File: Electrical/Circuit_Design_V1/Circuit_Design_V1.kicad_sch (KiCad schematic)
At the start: 0 parts

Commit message: #3 Improving the coincell battery holder symbol.
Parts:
- added P1: ~, symbol Etchasketch_hardware_symbol_library:20mm_Coin_Cell_Breakout_Board_(CR2032)
- added U1: STM32G474RETx, Package_QFP:LQFP-64_10x10mm_P0.5mm, symbol MCU_ST_STM32G4:STM32G474RETx
- added U2: ~, symbol Etchasketch_hardware_symbol_library:4.2{dblquote}_300x400_Tri-Color_eInk_/_ePap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
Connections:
- new net: U1.15 (VSS), U1.31 (VSS), U1.47 (VSS), U1.63 (VSS)

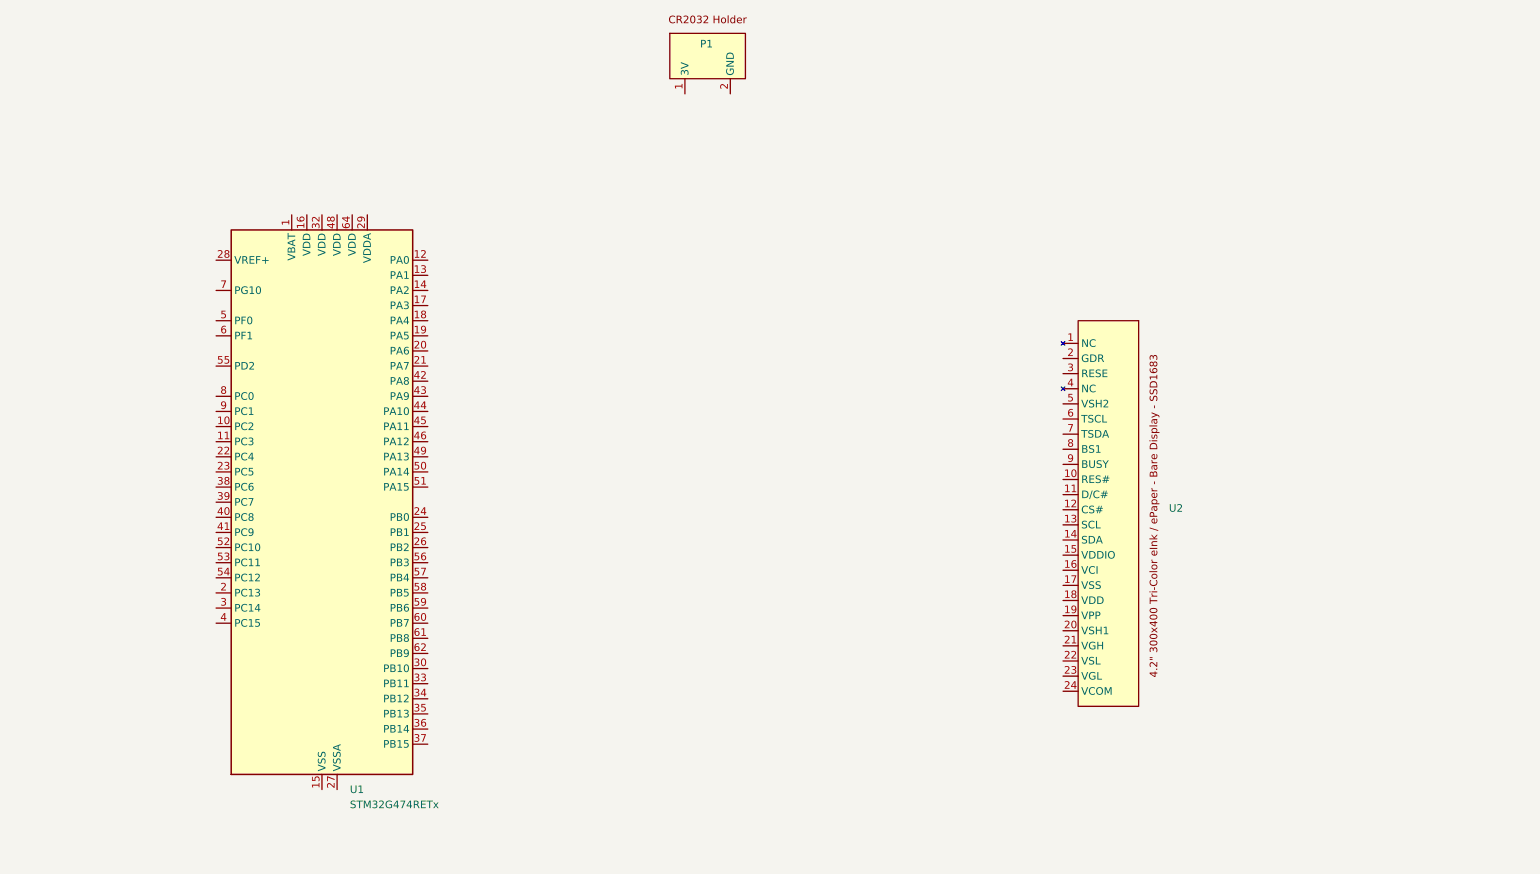
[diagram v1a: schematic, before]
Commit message: #3 Connecting MCU connectors to E-Ink on schematic.
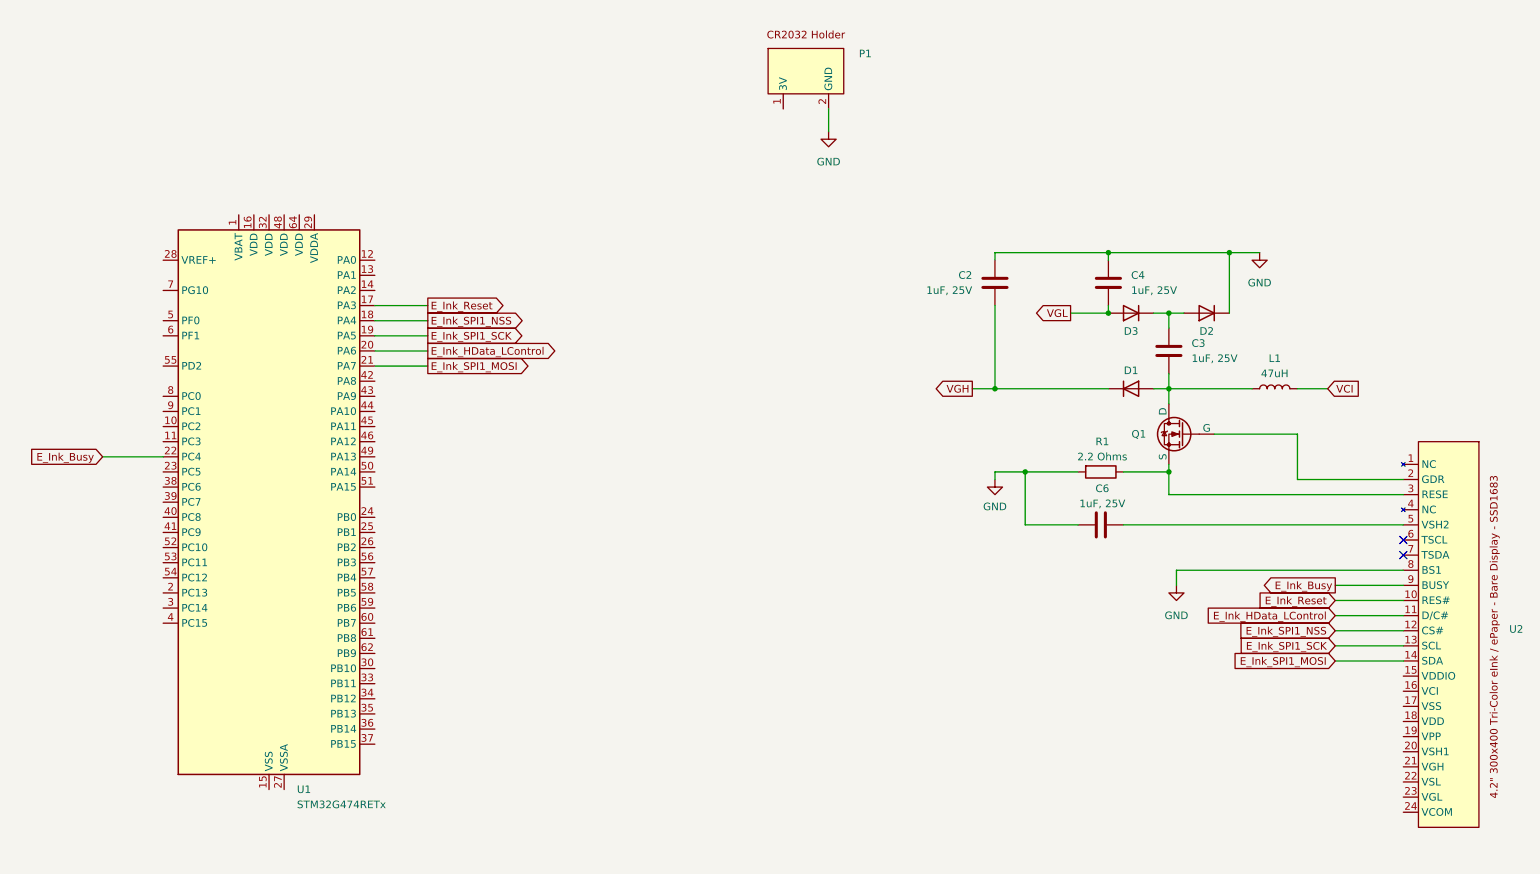
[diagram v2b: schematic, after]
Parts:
- added C2, C3, C4, C6: 1uF, 25V, symbol Device:C
- added D1, D2, D3: D, symbol Device:D
- added L1: 47uH, symbol Device:L
- added Q1: NMOS, symbol Simulation_SPICE:NMOS
- added R1: 2.2 Ohms, symbol Device:R
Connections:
- net GND: now reaches P1.2 (GND)
- net GND: now also U2.8 (BS1), C2.2, C4.2, C6.1, D2.1 (K), R1.2
- net E_Ink_Reset: now reaches U1.17 (PA3)
- net E_Ink_Reset: now also U2.10 (RES#)
- net E_Ink_SPI1_NSS: now reaches U1.18 (PA4)
- net E_Ink_SPI1_NSS: now also U2.12 (CS#)
- net E_Ink_SPI1_SCK: now reaches U1.19 (PA5)
- net E_Ink_SPI1_SCK: now also U2.13 (SCL)
- net E_Ink_HData_LControl: now reaches U1.20 (PA6)
- net E_Ink_HData_LControl: now also U2.11 (D/C#)
- net E_Ink_SPI1_MOSI: now reaches U1.21 (PA7)
- net E_Ink_SPI1_MOSI: now also U2.14 (SDA)
- net E_Ink_Busy: now reaches U1.22 (PC4)
- net E_Ink_Busy: now also U2.9 (BUSY)
- net at U2.2 (GDR): now also Q1.2 (G)
- net at U2.3 (RESE): now also Q1.3 (S), R1.1
- net at U2.5 (VSH2): now also C6.2
- new net: C3.1, D1.2 (A), L1.1, Q1.1 (D)
- new net: C3.2, D2.2 (A), D3.1 (K)
- new net VCI: L1.2
- new net VGH: C2.1, D1.1 (K)
- new net VGL: C4.1, D3.2 (A)
- no-connect marks 0 -> 2
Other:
- moved on the sheet: U1, U2
